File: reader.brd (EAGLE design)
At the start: 52.2 x 34 mm, 14 parts, among them J1 RJ11-6PTH, J2 AVR_SPI_PRG_6NS

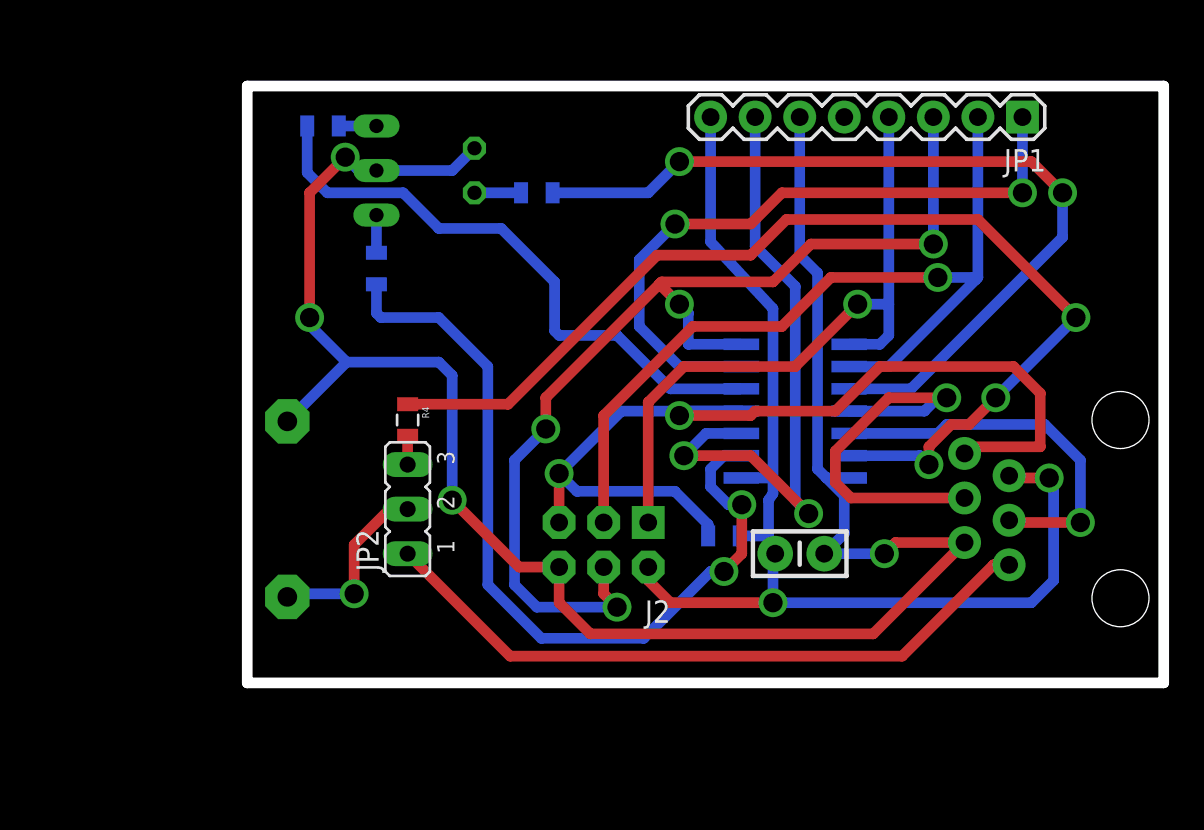
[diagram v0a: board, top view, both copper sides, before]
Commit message: Clean all connections from the board
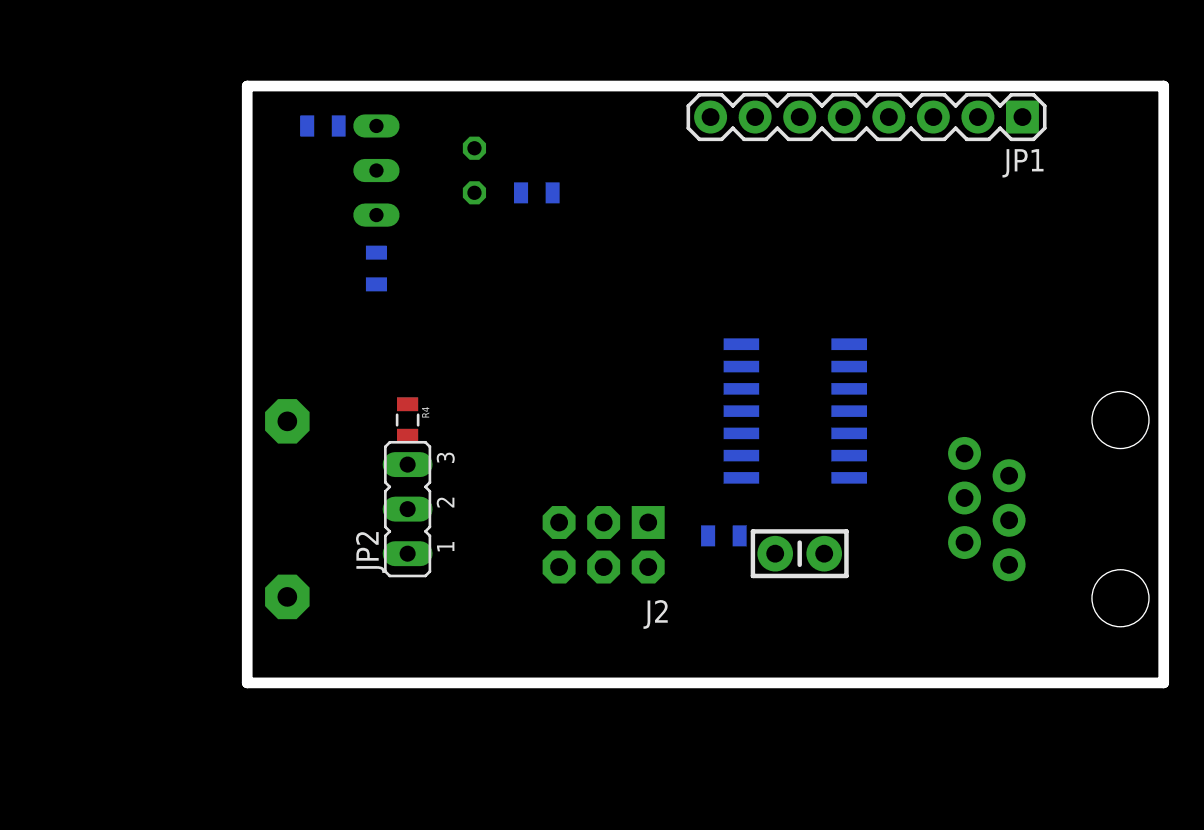
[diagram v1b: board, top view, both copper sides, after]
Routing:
- net GND: track 111.5 -> 0.00 mm, vias 4 -> 0
- net VCC: track 65.9 -> 0.00 mm, vias 2 -> 0
- net SPEAKER: track 62.0 -> 0.00 mm, vias 3 -> 0
- net MOSI: track 60.5 -> 0.00 mm, vias 4 -> 0
- net RST: track 58.8 -> 0.00 mm, vias 2 -> 0
- net SCK: track 49.2 -> 0.00 mm, vias 1 -> 0
- net BLUE_LED: track 48.8 -> 0.00 mm, vias 2 -> 0
- net RED_LED: track 47.5 -> 0.00 mm, vias 2 -> 0
- net EXT_SPEAKER: track 38.9 -> 0.00 mm
- net RDR_SS: track 38.3 -> 0.00 mm, vias 2 -> 0
- net MISO: track 37.8 -> 0.00 mm, vias 1 -> 0
- net RDR_RESET: track 36.2 -> 0.00 mm, vias 2 -> 0
- net GREEN_LED: track 34.2 -> 0.00 mm
- net CONTROLLER_RXD: track 23.0 -> 0.00 mm, vias 1 -> 0
- net CONTROLLER_TXD: track 21.9 -> 0.00 mm, vias 1 -> 0
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
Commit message: Add a switch transistor to drive the speaker
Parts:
- added R6: 160R, SparkFun-Passives:0805
- added T1: BC547, transistor:TO92
- R4: value 66R -> 1K8
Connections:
- removed net N$9: JP2.3, R4.2
- new net N$4: R4.2, T1.2
- new net N$5: R6.1, T1.1
- new net N$7: JP2.3, R6.2
- net VCC: now also T1.3
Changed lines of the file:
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@@
 <element name="R2" library="SparkFun-Passives" package="0805" value="360R" x="4.318" y="31.75" rot="MR0"/>
 <element name="R3" library="SparkFun-Passives" package="0805" value="680R" x="16.51" y="27.94" rot="MR0"/>
-<element name="R4" library="SparkFun-Passives" package="0805" value="66R" x="9.144" y="14.986" rot="R270"/>
+<element name="R4" library="SparkFun-Passives" package="0805" value="1K8" x="9.144" y="14.986" rot="R270"/>
 <element name="R5" library="SparkFun-Passives" package="0805" value="4K7" x="27.178" y="8.382" rot="MR0"/>
 <element name="SP1" library="buzzer" package="AL23P" value="AL23P" x="2.286" y="9.906" rot="MR90">
@@
 </element>
 <element name="U$1" library="attiny841" package="SO14" value="TINY841" x="31.242" y="15.494" rot="MR90"/>
+<element name="T1" library="transistor" package="TO92" value="BC547" x="-6.604" y="-4.699"/>
+<element name="R6" library="SparkFun-Passives" package="0805" value="160R" x="-10.795" y="-4.572"/>
 </elements>
 <signals>
@@
 <contactref element="JP1" pad="8"/>
 <contactref element="J2" pad="2"/>
+<contactref element="T1" pad="3"/>
 <wire x1="28.1686" y1="11.684" x2="26.416" y2="32.258" width="0" layer="19" extent="16-16"/>
 <wire x1="28.078" y1="8.382" x2="28.1686" y2="11.684" width="0" layer="19" extent="16-16"/>
@@
 <wire x1="22.86" y1="6.604" x2="28.078" y2="8.382" width="0" layer="19" extent="16-16"/>
 <wire x1="43.434" y1="11.811" x2="30.099" y2="7.366" width="0" layer="19" extent="1-1"/>
+<wire x1="-7.874" y1="-4.699" x2="22.86" y2="6.604" width="0" layer="19" extent="1-1"/>
 </signal>
 <signal name="GND">
@@
 <wire x1="9.144" y1="15.886" x2="34.3154" y2="12.954" width="0" layer="19" extent="1-16"/>
 </signal>
-<signal name="N$9">
-<contactref element="R4" pad="2"/>
-<contactref element="JP2" pad="3"/>
-<wire x1="9.144" y1="12.446" x2="9.144" y2="14.086" width="0" layer="19" extent="1-1"/>
-</signal>
 <signal name="N$1">
 <contactref element="SP1" pad="1"/>
@@
 <wire x1="2.286" y1="4.9022" x2="9.144" y2="9.906" width="0" layer="19" extent="1-1"/>
 </signal>
+<signal name="N$4">
+<contactref element="R4" pad="2"/>
+<contactref element="T1" pad="2"/>
+<wire x1="-6.604" y1="-2.794" x2="9.144" y2="14.086" width="0" layer="19" extent="1-1"/>
+</signal>
+<signal name="N$5">
+<contactref element="T1" pad="1"/>
+<contactref element="R6" pad="1"/>
+<wire x1="-5.334" y1="-4.699" x2="-11.695" y2="-4.572" width="0" layer="19" extent="1-1"/>
+</signal>
+<signal name="N$7">
+<contactref element="JP2" pad="3"/>
+<contactref element="R6" pad="2"/>
+<wire x1="-9.895" y1="-4.572" x2="9.144" y2="12.446" width="0" layer="19" extent="1-1"/>
+</signal>
 </signals>

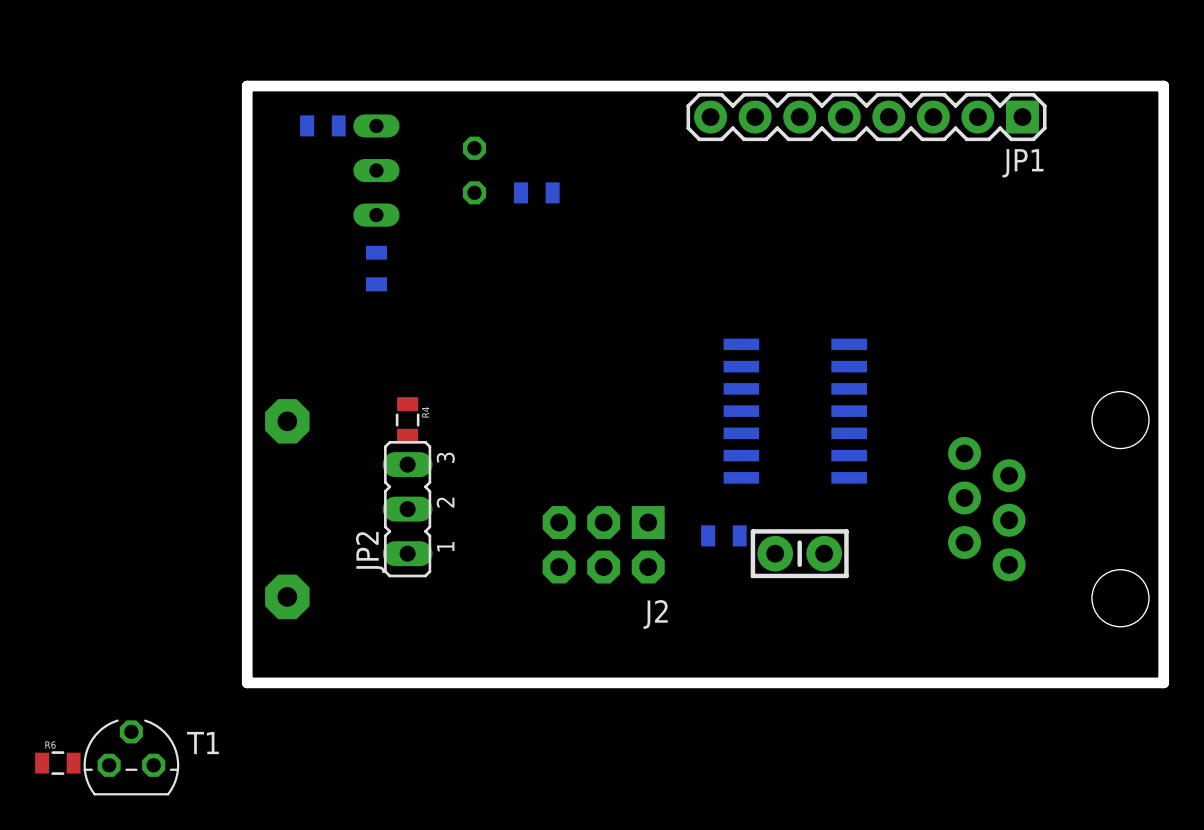
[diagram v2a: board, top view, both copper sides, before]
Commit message: Swap SPEAKER and BLUE_LED, reorganize components
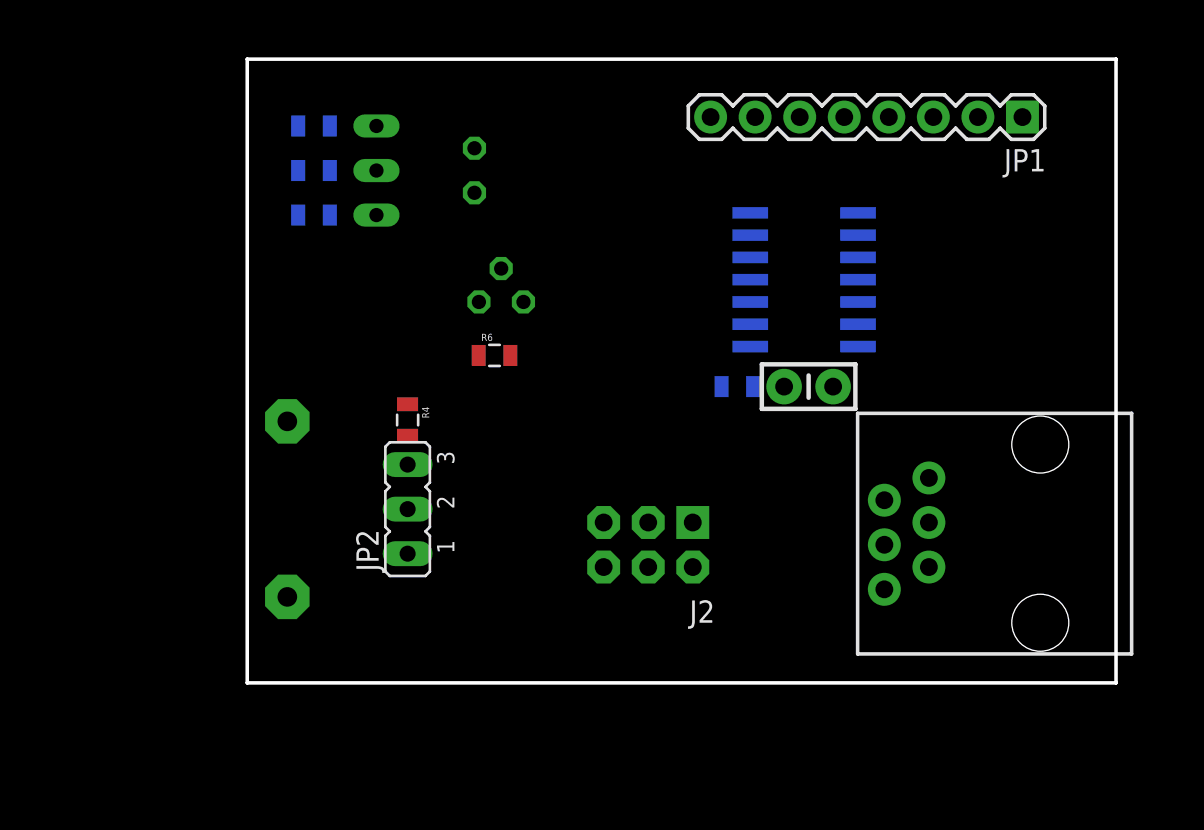
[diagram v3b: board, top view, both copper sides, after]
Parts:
- moved R6 34.1 mm to (14.1, 18.7)
- moved T1 33.8 mm to (14.5, 21.7), flipped to the bottom
- moved R3 12.8 mm to (3.81, 29.2), turned to 180 degrees
- moved J1 12.4 mm to (45.2, 3.43), flipped to the top, turned to 90 degrees
- moved C1 9.54 mm to (32.0, 16.9)
- moved R5 8.54 mm to (27.9, 16.9)
- moved U$1 7.51 mm to (31.8, 23.0)
- moved R1 4.68 mm to (3.81, 26.7), turned to 0 degrees
- moved J2 2.54 mm to (22.9, 7.87)
- moved R2 0.51 mm to (3.81, 31.8)
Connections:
- net BLUE_LED: now also U$1.13; no longer U$1.10
- net SPEAKER: now also U$1.10; no longer U$1.13
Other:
- board size 52.2 x 34 mm -> 49.5 x 35.6 mm

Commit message: [WIP] Manually route few connectors on the board
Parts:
- removed LD1: STATUS, led:DUOLED-C-5MM
- removed U$1: TINY841, attiny841:SO14
- added LED2: STATUS, led:DUOLED-C-5MM
- added U1: TINY841, attiny841:SO14
- moved R4 10.8 mm to (16.5, 22.9), turned to 0 degrees
- moved T1 1.93 mm to (12.7, 21.0), flipped to the top
- moved R6 1.53 mm to (14.0, 17.1), turned to 270 degrees
- moved J1 1.02 mm to (45.7, 2.54)
- moved JP1 0.80 mm to (44.5, 33.0)
- moved JP2 0.46 mm to (9.53, 10.2)
- moved C1 0.46 mm to (31.8, 16.5)
- moved R5 0.38 mm to (27.9, 16.5)
- moved SP1 0.36 mm to (2.54, 10.2), flipped to the top
- moved LED1 0.25 mm to (12.7, 29.2), flipped to the top
- moved J2 0.25 mm to (22.9, 7.62)
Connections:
- net BLUE_LED: now also U1.13; no longer U$1.13
- net CONTROLLER_RXD: now also U1.11; no longer U$1.11
- net CONTROLLER_TXD: now also U1.12; no longer U$1.12
- net GND: now also LED2.C, U1.14; no longer LD1.C, U$1.14
- net GREEN_LED: now also U1.5; no longer U$1.5
- net MISO: now also U1.8; no longer U$1.8
- net MOSI: now also U1.7; no longer U$1.7
- net N$2: now also LED2.AR; no longer LD1.AR
- net N$3: now also LED2.AX; no longer LD1.AX
- net RDR_RESET: now also U1.3; no longer U$1.3
- net RDR_SS: now also U1.6; no longer U$1.6
- net RED_LED: now also U1.2; no longer U$1.2
- net RST: now also U1.4; no longer U$1.4
- net SCK: now also U1.9; no longer U$1.9
- net SPEAKER: now also U1.10; no longer U$1.10
- net VCC: now also U1.1; no longer U$1.1
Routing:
- net MOSI: track 0.00 -> 81.2 mm, vias 0 -> 2
- net VCC: track 0.00 -> 69.9 mm
- net GND: track 0.00 -> 54.5 mm, vias 0 -> 1
- net EXT_SPEAKER: track 0.00 -> 51.2 mm, vias 0 -> 1
- net SCK: track 0.00 -> 42.6 mm, vias 0 -> 2
- net MISO: track 0.00 -> 42.3 mm, vias 0 -> 2
- net RDR_SS: track 0.00 -> 36.0 mm
- net CONTROLLER_RXD: track 0.00 -> 28.9 mm, vias 0 -> 2
- net RST: track 0.00 -> 27.9 mm
- net RDR_RESET: track 0.00 -> 23.5 mm
- net CONTROLLER_TXD: track 0.00 -> 20.2 mm
- net N$1: track 0.00 -> 9.06 mm
- net N$7: track 0.00 -> 6.50 mm
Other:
- board size 49.5 x 35.6 mm -> 49.5 x 36.8 mm
- board text added: "* *-* internal *-* * external"
- board text added: "ISP header"
- board text added: "LED2"
- board text added: "Read"
- board text added: "Status"

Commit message: Reroute the board
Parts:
- moved R4 3.18 mm to (14.0, 24.8), turned to 180 degrees
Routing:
- net BLUE_LED: track 0.00 -> 77.0 mm
- net RST: track 27.9 -> 69.9 mm, vias 0 -> 2
- net GREEN_LED: track 0.00 -> 28.9 mm
- net RED_LED: track 0.00 -> 28.4 mm
- net SPEAKER: track 0.00 -> 24.2 mm, vias 0 -> 1
- net VCC: track 69.9 -> 84.7 mm
- net N$6: track 0.00 -> 8.50 mm
- net GND: track 54.5 -> 60.3 mm
- net N$2: track 0.00 -> 3.00 mm
- net N$3: track 0.00 -> 2.98 mm
- net N$5: track 0.00 -> 2.92 mm
- net N$4: track 0.00 -> 2.06 mm
- added copper zone on layer 1, net GND
- added copper zone on layer 16, net GND
